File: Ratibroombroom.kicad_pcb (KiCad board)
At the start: 2 copper layers, 40 x 60 mm, 0 parts

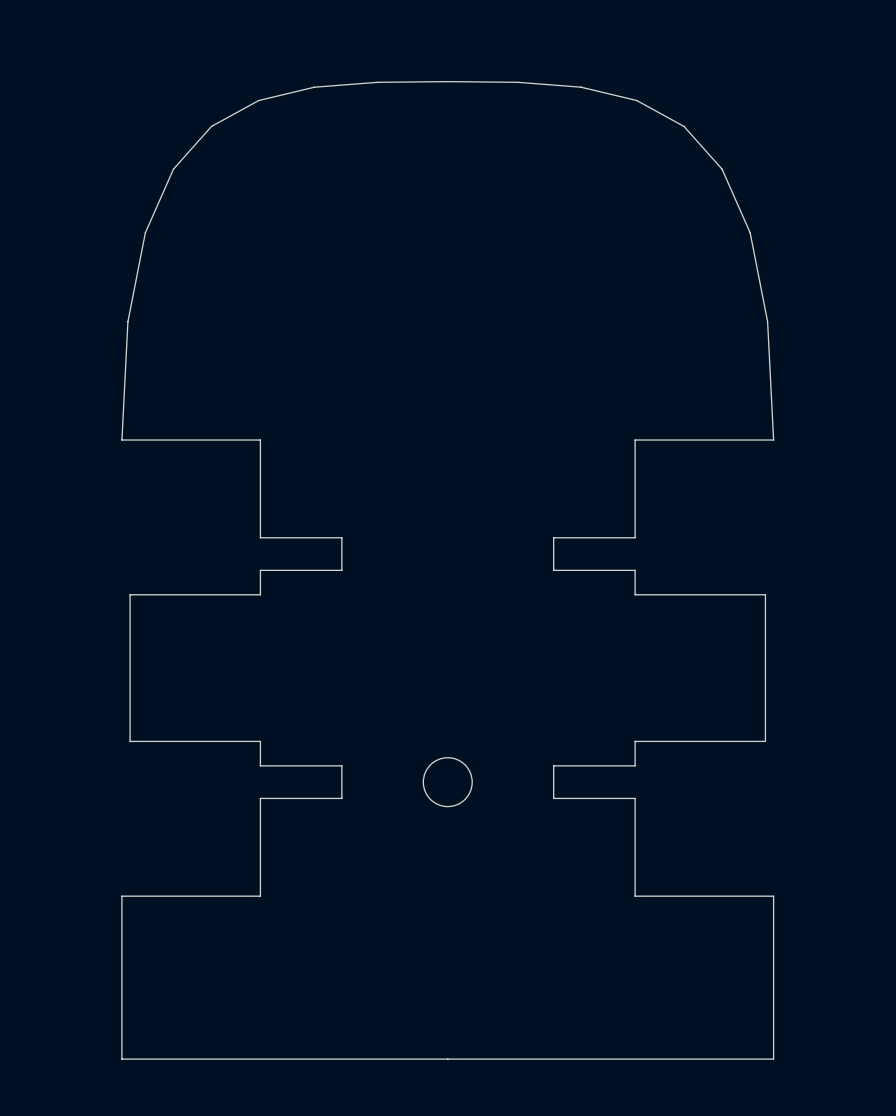
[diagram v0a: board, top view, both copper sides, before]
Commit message: Modify board to 45mm width to make everything fit. Place components in pcbnew Modify schematic to merge I2C, SWIO and UART connectors into a single 2x5 pin connector
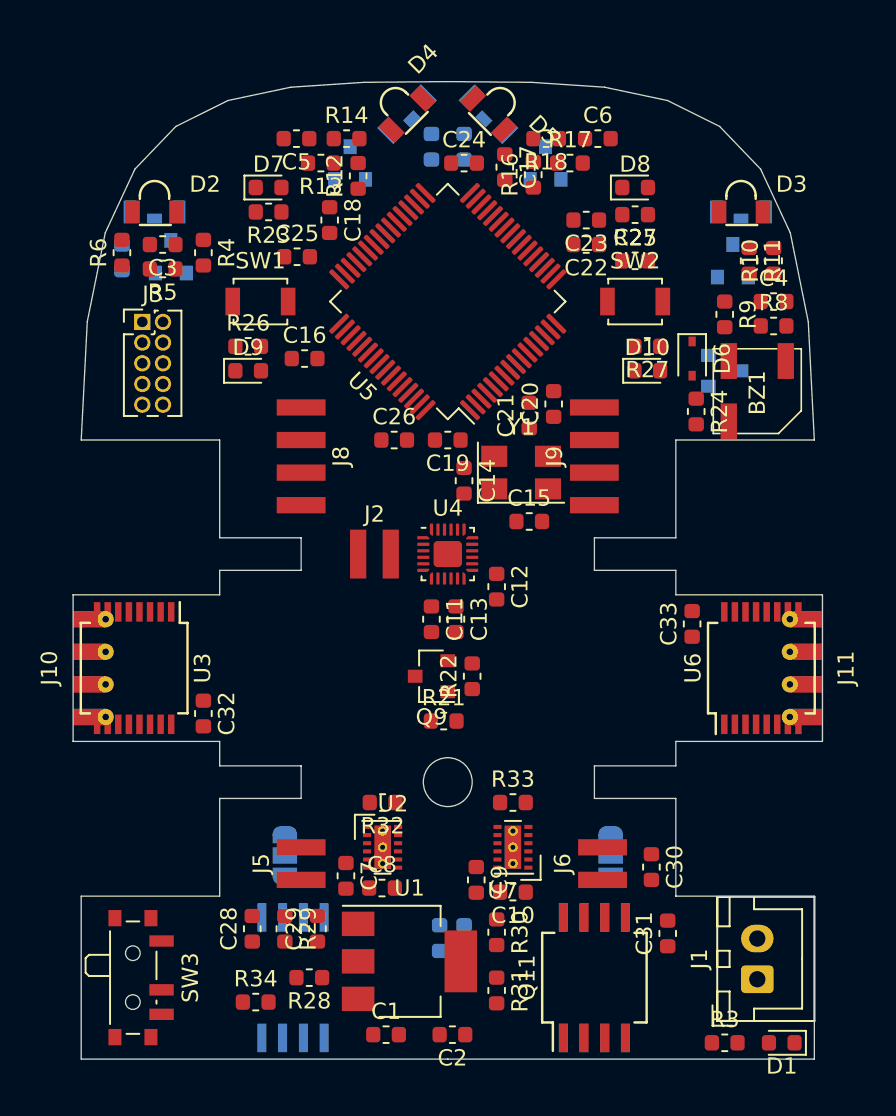
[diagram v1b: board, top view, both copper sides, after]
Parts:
- added BZ1: MLT5020, Ratibroombroom:MLT-5020, F.Cu at (164.0, 81.0)
- added C1: 1u, Capacitor_SMD:C_0603_1608Metric, F.Cu at (141.2, 120.5)
- added C10: 10u, Capacitor_SMD:C_0603_1608Metric, F.Cu at (149.0, 111.8)
- added C11: 10n, Capacitor_SMD:C_0603_1608Metric, F.Cu at (144.0, 95.0)
- added C12: 100n, Capacitor_SMD:C_0603_1608Metric, F.Cu at (148.0, 93.0)
- added C13: 100n, Capacitor_SMD:C_0603_1608Metric, F.Cu at (145.5, 95.0)
- added C14: 20p, Capacitor_SMD:C_0603_1608Metric, F.Cu at (146.0, 86.5)
- added C15: 20p, Capacitor_SMD:C_0603_1608Metric, F.Cu at (150.0, 89.0)
- added C16: 10n, Capacitor_SMD:C_0603_1608Metric, F.Cu at (136.2, 79.0)
- added C17: 2.2u, Capacitor_SMD:C_0603_1608Metric, F.Cu at (148.5, 67.2)
- added C18: 2.2u, Capacitor_SMD:C_0603_1608Metric, F.Cu at (137.8, 70.5)
- added C19: 100n, Capacitor_SMD:C_0603_1608Metric, F.Cu at (145.0, 84.0)
- added C2: 1u, Capacitor_SMD:C_0603_1608Metric, F.Cu at (145.3, 120.5)
- added C20: 100n, Capacitor_SMD:C_0603_1608Metric, F.Cu at (151.5, 81.8)
- added C21: 1u, Capacitor_SMD:C_0603_1608Metric, F.Cu at (150.0, 82.5)
- added C22: 100n, Capacitor_SMD:C_0603_1608Metric, F.Cu at (153.5, 72.0)
- added C23: 4.7u, Capacitor_SMD:C_0603_1608Metric, F.Cu at (153.5, 70.5)
- added C24: 100n, Capacitor_SMD:C_0603_1608Metric, F.Cu at (146.0, 67.0)
- added C25: 100n, Capacitor_SMD:C_0603_1608Metric, F.Cu at (135.8, 72.8)
- added C26: 100n, Capacitor_SMD:C_0603_1608Metric, F.Cu at (141.7, 84.0)
- added C27: 10n, Capacitor_SMD:C_0603_1608Metric, F.Cu at (156.5, 73.0)
- added C28: 10u, Capacitor_SMD:C_0603_1608Metric, F.Cu at (133.0, 114.0)
- added C29: 10u, Capacitor_SMD:C_0603_1608Metric, F.Cu at (137.0, 114.0)
- added C3: 1u, Capacitor_SMD:C_0603_1608Metric, F.Cu at (127.5, 72.0)
- added C30: 10u, Capacitor_SMD:C_0603_1608Metric, F.Cu at (157.5, 110.2)
- added C31: 10u, Capacitor_SMD:C_0603_1608Metric, F.Cu at (158.5, 114.3)
- added C32: 100n, Capacitor_SMD:C_0603_1608Metric, F.Cu at (130.0, 100.8)
- added C33: 100n, Capacitor_SMD:C_0603_1608Metric, F.Cu at (160.0, 95.3)
- added C4: 1u, Capacitor_SMD:C_0603_1608Metric, F.Cu at (165.0, 75.5)
- added C5: 1u, Capacitor_SMD:C_0603_1608Metric, F.Cu at (135.7, 65.5)
- added C6: 1u, Capacitor_SMD:C_0603_1608Metric, F.Cu at (154.2, 65.5)
- added C7: 100n, Capacitor_SMD:C_0603_1608Metric, F.Cu at (138.8, 110.8)
- added C8: 10u, Capacitor_SMD:C_0603_1608Metric, F.Cu at (141.0, 111.5)
- added C9: 100n, Capacitor_SMD:C_0603_1608Metric, F.Cu at (146.8, 111.0)
- added D1: LED, LED_SMD:LED_0603_1608Metric, F.Cu at (165.5, 121.0)
- added D10: LED, LED_SMD:LED_0603_1608Metric, F.Cu at (157.2, 79.8)
- added D2: SFH4045N, Ratibroombroom:SFH4045N, F.Cu at (127.0, 70.0)
- added D3: SFH4045N, Ratibroombroom:SFH4045N, F.Cu at (163.0, 70.0)
- added D4: SFH4045N, Ratibroombroom:SFH4045N, F.Cu at (142.5, 64.0)
- added D5: SFH4045N, Ratibroombroom:SFH4045N, F.Cu at (147.5, 64.0)
- added D6: 1N4148, Diode_SMD:D_SOD-323, F.Cu at (160.0, 79.0)
- added D7: LED, LED_SMD:LED_0603_1608Metric, F.Cu at (134.0, 68.5)
- added D8: LED, LED_SMD:LED_0603_1608Metric, F.Cu at (156.5, 68.5)
- added D9: LED, LED_SMD:LED_0603_1608Metric, F.Cu at (132.8, 79.8)
- added J1: Conn_01x02_Male, Connector_JST:JST_XH_B2B-XH-A_1x02_P2.50mm_Vertical, F.Cu at (164.0, 117.1)
- added J10: Conn_01x04_Male, Ratibroombroom:Edge_connector_4P_1x3mm, F.Cu at (123.0, 98.0)
- added J11: Conn_01x04_Male, Ratibroombroom:Edge_connector_4P_1x3mm, F.Cu at (167.0, 98.0)
- added J2: Conn_01x02_Male, Ratibroombroom:Pad_SMD_2P_1x3mm, F.Cu at (140.5, 91.0)
- added J3: Conn_01x10_Male, Connector_PinHeader_1.27mm:PinHeader_2x05_P1.27mm_Vertical, F.Cu at (126.2, 76.8)
- added J5: Conn_01x02_Male, Ratibroombroom:Pad_SMD_2P_1x3mm, F.Cu at (136.0, 110.0)
- added J6: Conn_01x02_Male, Ratibroombroom:Pad_SMD_2P_1x3mm, F.Cu at (154.5, 110.0)
- added J8: Conn_01x04_Male, Ratibroombroom:Pad_SMD_4P_1x3mm, F.Cu at (136.0, 85.0)
- added J9: Conn_01x04_Male, Ratibroombroom:Pad_SMD_4P_1x3mm, F.Cu at (154.0, 85.0)
- added JP1: Jumper_NC_Dual, Jumper:SolderJumper-3_P1.3mm_Open_RoundedPad1.0x1.5mm_NumberLabels, B.Cu at (135.0, 109.5)
- added JP2: Jumper_NC_Dual, Jumper:SolderJumper-3_P1.3mm_Open_RoundedPad1.0x1.5mm_NumberLabels, B.Cu at (155.0, 109.5)
- added Q1: IRLML6344, Package_TO_SOT_SMD:SOT-23, B.Cu at (128.0, 72.8)
- added Q10: S8050, Package_TO_SOT_SMD:SOT-23, B.Cu at (162.0, 79.8)
- added Q11: IRF7416PbF, Package_SO:SO-8_5.3x6.2mm_P1.27mm, F.Cu at (154.0, 117.0)
- added Q2: IRLML6344, Package_TO_SOT_SMD:SOT-23, B.Cu at (162.5, 73.0)
- added Q3: IRLML6344, Package_TO_SOT_SMD:SOT-23, B.Cu at (139.0, 67.0)
- added Q4: IRLML6344, Package_TO_SOT_SMD:SOT-23, B.Cu at (151.0, 67.0)
- added Q5: PT12-21B/TR8, Ratibroombroom:PT12-21B-TR8, B.Cu at (127.0, 70.0)
- added Q6: PT12-21B/TR8, Ratibroombroom:PT12-21B-TR8, B.Cu at (163.0, 70.0)
- added Q7: PT12-21B/TR8, Ratibroombroom:PT12-21B-TR8, B.Cu at (142.5, 64.0)
- added Q8: PT12-21B/TR8, Ratibroombroom:PT12-21B-TR8, B.Cu at (147.5, 64.0)
- added Q9: IRLML6344, Package_TO_SOT_SMD:SOT-23, F.Cu at (144.0, 98.5)
- added R1: 47k, Resistor_SMD:R_0603_1608Metric, B.Cu at (146.0, 114.6)
- added R10: R, Resistor_SMD:R_0603_1608Metric, F.Cu at (165.0, 73.0)
- added R11: R, Resistor_SMD:R_0603_1608Metric, F.Cu at (163.5, 73.0)
- added R12: 100, Resistor_SMD:R_0603_1608Metric, F.Cu at (139.5, 67.8)
- added R13: 100k, Resistor_SMD:R_0603_1608Metric, F.Cu at (137.2, 67.0)
- added R14: R, Resistor_SMD:R_0603_1608Metric, F.Cu at (138.8, 65.5)
- added R15: R, Resistor_SMD:R_0603_1608Metric, B.Cu at (144.0, 66.0)
- added R16: 100, Resistor_SMD:R_0603_1608Metric, F.Cu at (150.2, 67.7)
- added R17: 100k, Resistor_SMD:R_0603_1608Metric, F.Cu at (152.5, 67.0)
- added R18: R, Resistor_SMD:R_0603_1608Metric, F.Cu at (151.0, 65.5)
- added R19: R, Resistor_SMD:R_0603_1608Metric, B.Cu at (146.0, 66.0)
- added R2: 26.1k, Resistor_SMD:R_0603_1608Metric, B.Cu at (144.5, 114.6)
- added R21: 100, Resistor_SMD:R_0603_1608Metric, F.Cu at (144.8, 101.2)
- added R22: 10k, Resistor_SMD:R_0603_1608Metric, F.Cu at (146.5, 98.5)
- added R23: 100, Resistor_SMD:R_0603_1608Metric, F.Cu at (134.0, 70.0)
- added R24: 10k, Resistor_SMD:R_0603_1608Metric, F.Cu at (160.2, 82.2)
- added R25: 100, Resistor_SMD:R_0603_1608Metric, F.Cu at (156.5, 70.2)
- added R26: 100, Resistor_SMD:R_0603_1608Metric, F.Cu at (132.8, 78.2)
- added R27: 100, Resistor_SMD:R_0603_1608Metric, F.Cu at (157.2, 78.2)
- added R28: 5.6k, Resistor_SMD:R_0603_1608Metric, F.Cu at (136.5, 117.0)
- added R29: 1.8k, Resistor_SMD:R_0603_1608Metric, F.Cu at (135.0, 114.0)
- added R3: 10k, Resistor_SMD:R_0603_1608Metric, F.Cu at (162.0, 121.0)
- added R30: 5.6k, Resistor_SMD:R_0603_1608Metric, F.Cu at (148.0, 114.2)
- added R31: 1.8k, Resistor_SMD:R_0603_1608Metric, F.Cu at (148.0, 117.8)
- added R32: 10k, Resistor_SMD:R_0603_1608Metric, F.Cu at (141.0, 106.2)
- added R33: 10k, Resistor_SMD:R_0603_1608Metric, F.Cu at (149.0, 106.2)
- added R34: 10k, Resistor_SMD:R_0603_1608Metric, F.Cu at (133.2, 118.5)
- added R4: 100, Resistor_SMD:R_0603_1608Metric, F.Cu at (130.0, 72.5)
- added R5: 100k, Resistor_SMD:R_0603_1608Metric, F.Cu at (127.5, 73.5)
- added R6: R, Resistor_SMD:R_0603_1608Metric, F.Cu at (125.0, 72.5)
- added R7: R, Resistor_SMD:R_0603_1608Metric, B.Cu at (125.0, 72.8)
- added R8: 100, Resistor_SMD:R_0603_1608Metric, F.Cu at (165.0, 77.0)
- added R9: 100k, Resistor_SMD:R_0603_1608Metric, F.Cu at (162.0, 76.3)
- added SW1: B3U, Button_Switch_SMD:SW_SPST_B3U-1000P, F.Cu at (133.5, 75.5)
- added SW2: B3U, Button_Switch_SMD:SW_SPST_B3U-1000P, F.Cu at (156.5, 75.5)
- added SW3: PCM12, Button_Switch_SMD:SW_SPDT_PCM12, F.Cu at (126.0, 117.0)
- added U1: AZ1117-3.3, Package_TO_SOT_SMD:SOT-223-3_TabPin2, F.Cu at (142.7, 116.0)
- added U2: DRV8835, Package_SON:WSON-12-1EP_3x2mm_P0.5mm_EP1x2.65_ThermalVias, F.Cu at (141.0, 109.0)
- added U3: AS5145B-HSST, Package_SO:SSOP-16_5.3x6.2mm_P0.65mm, F.Cu at (125.8, 98.0)
- added U4: MPU-9250, Package_DFN_QFN:QFN-24-1EP_3x3mm_P0.4mm_EP1.75x1.6mm, F.Cu at (145.0, 91.0)
- added U5: STM32F405RGTx, Package_QFP:LQFP-64_10x10mm_P0.5mm, F.Cu at (145.0, 75.5)
- added U6: AS5145B-HSST, Package_SO:SSOP-16_5.3x6.2mm_P0.65mm, F.Cu at (164.2, 98.0)
- added U7: DRV8835, Package_SON:WSON-12-1EP_3x2mm_P0.5mm_EP1x2.65_ThermalVias, F.Cu at (149.0, 109.0)
- added U8: L6932D1.2TR, Package_SO:SO-8_5.3x6.2mm_P1.27mm, B.Cu at (135.5, 117.0)
- added U9: L6932D1.2TR, Package_SO:SO-8_5.3x6.2mm_P1.27mm, B.Cu at (154.0, 117.0)
- added Y1: 8MHZ, Crystal:Crystal_SMD_5032-4Pin_5.0x3.2mm, F.Cu at (149.5, 86.0)
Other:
- board size 40 x 60 mm -> 46 x 60 mm
- net class Default: clearance 0.2 -> 0.127; trace_width 0.25 -> 0.127; via_dia 0.8 -> 0.6; via_drill 0.4 -> 0.3
- rule trace_clearance: 0.2 -> 0.127
- rule trace_min: 0.2 -> 0.127

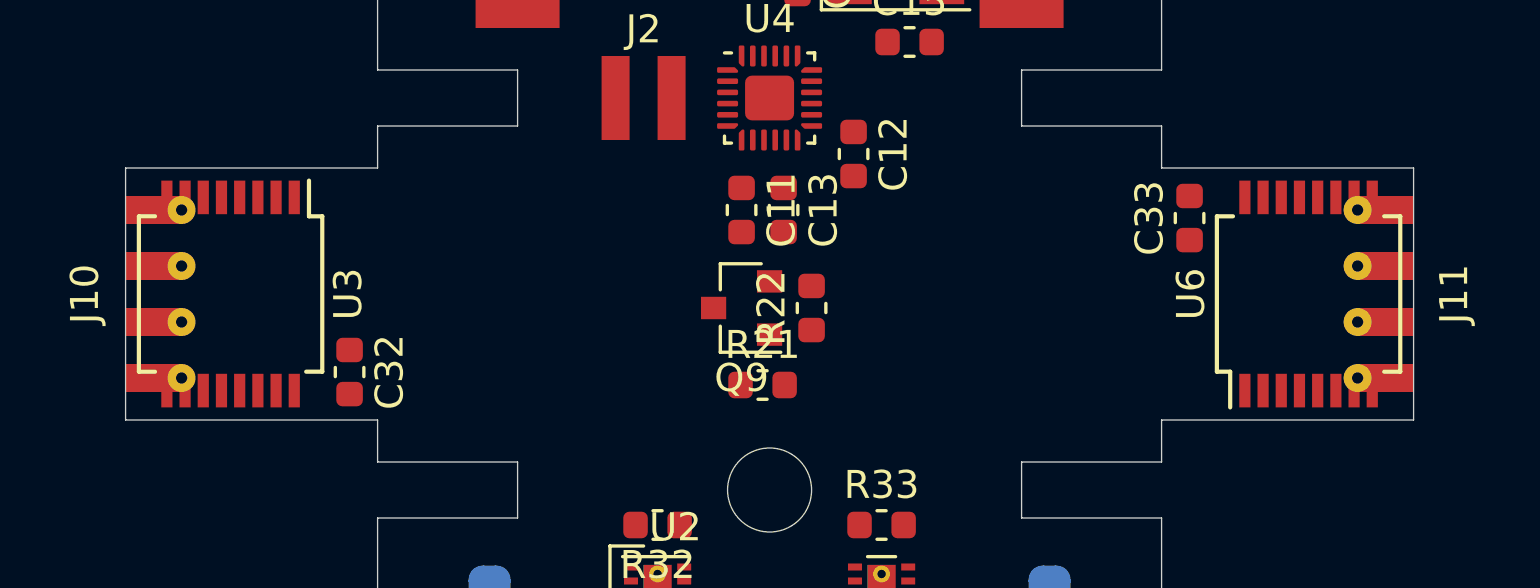
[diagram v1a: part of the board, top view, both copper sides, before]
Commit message: Change encoder board connector footprint to single side connector
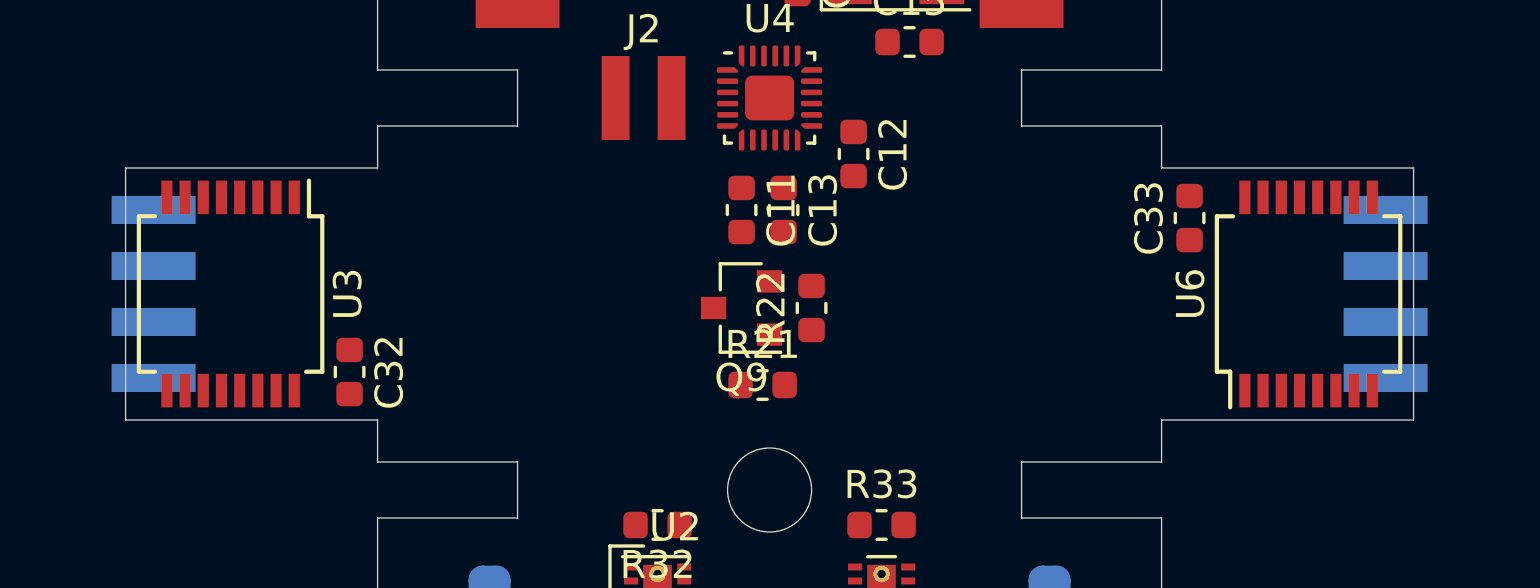
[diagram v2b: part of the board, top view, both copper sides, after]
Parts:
- J10, J11: footprint Ratibroombroom:Edge_connector_4P_1x3mm -> Ratibroombroom:Pad_SMD_4P_1x3mm; moved to B.Cu
- turned J10 to 270 degrees
- turned J11 to 90 degrees
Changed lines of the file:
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@@
     (add_net VBUS)
+  )
+  (module Ratibroombroom:Pad_SMD_4P_1x3mm (layer B.Cu)
+    (at 167 98 90)
+    (fp_text reference J11 (at 0 2.45 -90) (layer B.SilkS)
+      (effects (font (size 1 1) (thickness 0.15)) (justify mirror))
+    )
+    (fp_text value Conn_01x04_Male (at 0.05 4.05 -90) (layer B.Fab)
+      (effects (font (size 1 1) (thickness 0.15)) (justify mirror))
+    )
+    (pad 4 smd rect (at 3 0 90) (size 1 3) (layers B.Cu B.Mask)
+      (net 2 +3V3))
+    (pad 3 smd rect (at 1 0 90) (size 1 3) (layers B.Cu B.Mask)
+      (net 47 /R_DTEST1_A))
+    (pad 2 smd rect (at -1 0 90) (size 1 3) (layers B.Cu B.Mask)
+      (net 48 /R_DTEST2_B))
+    (pad 1 smd rect (at -3 0 90) (size 1 3) (layers B.Cu B.Mask)
+      (net 3 GND))
+  )
+  (module Ratibroombroom:Pad_SMD_4P_1x3mm (layer B.Cu)
+    (at 123 98 270)
+    (fp_text reference J10 (at 0 2.45 270) (layer B.SilkS)
+      (effects (font (size 1 1) (thickness 0.15)) (justify mirror))
+    )
+    (fp_text value Conn_01x04_Male (at 0.05 4.05 270) (layer B.Fab)
+      (effects (font (size 1 1) (thickness 0.15)) (justify mirror))
+    )
+    (pad 4 smd rect (at 3 0 270) (size 1 3) (layers B.Cu B.Mask)
+      (net 2 +3V3))
+    (pad 3 smd rect (at 1 0 270) (size 1 3) (layers B.Cu B.Mask)
+      (net 45 /L_DTEST1_A))
+    (pad 2 smd rect (at -1 0 270) (size 1 3) (layers B.Cu B.Mask)
+      (net 46 /L_DTEST2_B))
+    (pad 1 smd rect (at -3 0 270) (size 1 3) (layers B.Cu B.Mask)
+      (net 3 GND))
   )
   (module Connector_PinHeader_1.27mm:PinHeader_2x05_P1.27mm_Vertical (layer F.Cu)
@@
       ))
   )
-  (module Ratibroombroom:Edge_connector_4P_1x3mm (layer F.Cu)
-    (at 167 98 270)
-    (fp_text reference J11 (at 0 -2.45 90) (layer F.SilkS)
-      (effects (font (size 1 1) (thickness 0.15)))
-    )
-    (fp_text value Conn_01x04_Male (at 0.05 -4.05 90) (layer F.Fab)
-      (effects (font (size 1 1) (thickness 0.15)))
-    )
-    (pad 4 thru_hole circle (at 3 1 270) (size 1 1) (drill 0.4) (layers *.Cu *.Mask)
-      (net 2 +3V3))
-    (pad 3 thru_hole circle (at 1 1 270) (size 1 1) (drill 0.4) (layers *.Cu *.Mask)
-      (net 47 /R_DTEST1_A))
-    (pad 2 thru_hole circle (at -1 1 270) (size 1 1) (drill 0.4) (layers *.Cu *.Mask)
-      (net 48 /R_DTEST2_B))
-    (pad 1 thru_hole circle (at -3 1 270) (size 1 1) (drill 0.4) (layers *.Cu *.Mask)
-      (net 3 GND))
-    (pad 4 smd rect (at 3 0 270) (size 1 2) (layers *.Mask B.Cu)
-      (net 2 +3V3))
-    (pad 3 smd rect (at 1 0 270) (size 1 2) (layers *.Mask B.Cu)
-      (net 47 /R_DTEST1_A))
-    (pad 2 smd rect (at -1 0 270) (size 1 2) (layers *.Mask F.Cu)
-      (net 48 /R_DTEST2_B))
-    (pad 1 smd rect (at -3 0 270) (size 1 2) (layers *.Mask F.Cu)
-      (net 3 GND))
-    (pad 4 smd rect (at 3 0 270) (size 1 2) (layers *.Mask F.Cu)
-      (net 2 +3V3))
-    (pad 3 smd rect (at 1 0 270) (size 1 2) (layers *.Mask F.Cu)
-      (net 47 /R_DTEST1_A))
-    (pad 2 smd rect (at -1 0 270) (size 1 2) (layers *.Mask B.Cu)
-      (net 48 /R_DTEST2_B))
-    (pad 1 smd rect (at -3 0 270) (size 1 2) (layers *.Mask B.Cu)
-      (net 3 GND))
-  )
-  (module Ratibroombroom:Edge_connector_4P_1x3mm (layer F.Cu)
-    (at 123 98 90)
-    (fp_text reference J10 (at 0 -2.45 90) (layer F.SilkS)
-      (effects (font (size 1 1) (thickness 0.15)))
-    )
-    (fp_text value Conn_01x04_Male (at 0.05 -4.05 90) (layer F.Fab)
-      (effects (font (size 1 1) (thickness 0.15)))
-    )
-    (pad 4 thru_hole circle (at 3 1 90) (size 1 1) (drill 0.4) (layers *.Cu *.Mask)
-      (net 2 +3V3))
-    (pad 3 thru_hole circle (at 1 1 90) (size 1 1) (drill 0.4) (layers *.Cu *.Mask)
-      (net 45 /L_DTEST1_A))
-    (pad 2 thru_hole circle (at -1 1 90) (size 1 1) (drill 0.4) (layers *.Cu *.Mask)
-      (net 46 /L_DTEST2_B))
-    (pad 1 thru_hole circle (at -3 1 90) (size 1 1) (drill 0.4) (layers *.Cu *.Mask)
-      (net 3 GND))
-    (pad 4 smd rect (at 3 0 90) (size 1 2) (layers *.Mask B.Cu)
-      (net 2 +3V3))
-    (pad 3 smd rect (at 1 0 90) (size 1 2) (layers *.Mask B.Cu)
-      (net 45 /L_DTEST1_A))
-    (pad 2 smd rect (at -1 0 90) (size 1 2) (layers *.Mask F.Cu)
-      (net 46 /L_DTEST2_B))
-    (pad 1 smd rect (at -3 0 90) (size 1 2) (layers *.Mask F.Cu)
-      (net 3 GND))
-    (pad 4 smd rect (at 3 0 90) (size 1 2) (layers *.Mask F.Cu)
-      (net 2 +3V3))
-    (pad 3 smd rect (at 1 0 90) (size 1 2) (layers *.Mask F.Cu)
-      (net 45 /L_DTEST1_A))
-    (pad 2 smd rect (at -1 0 90) (size 1 2) (layers *.Mask B.Cu)
-      (net 46 /L_DTEST2_B))
-    (pad 1 smd rect (at -3 0 90) (size 1 2) (layers *.Mask B.Cu)
-      (net 3 GND))
-  )
   (module Ratibroombroom:Pad_SMD_4P_1x3mm (layer F.Cu)
